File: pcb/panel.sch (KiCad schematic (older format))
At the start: 15 parts, among them IC1 ATMEGA88P-20PU, P1 KEYBOARD, P2 SERIAL, P3 I2C, U1 C, U2 CP, U3 2X16DIGIT-DISPLAY

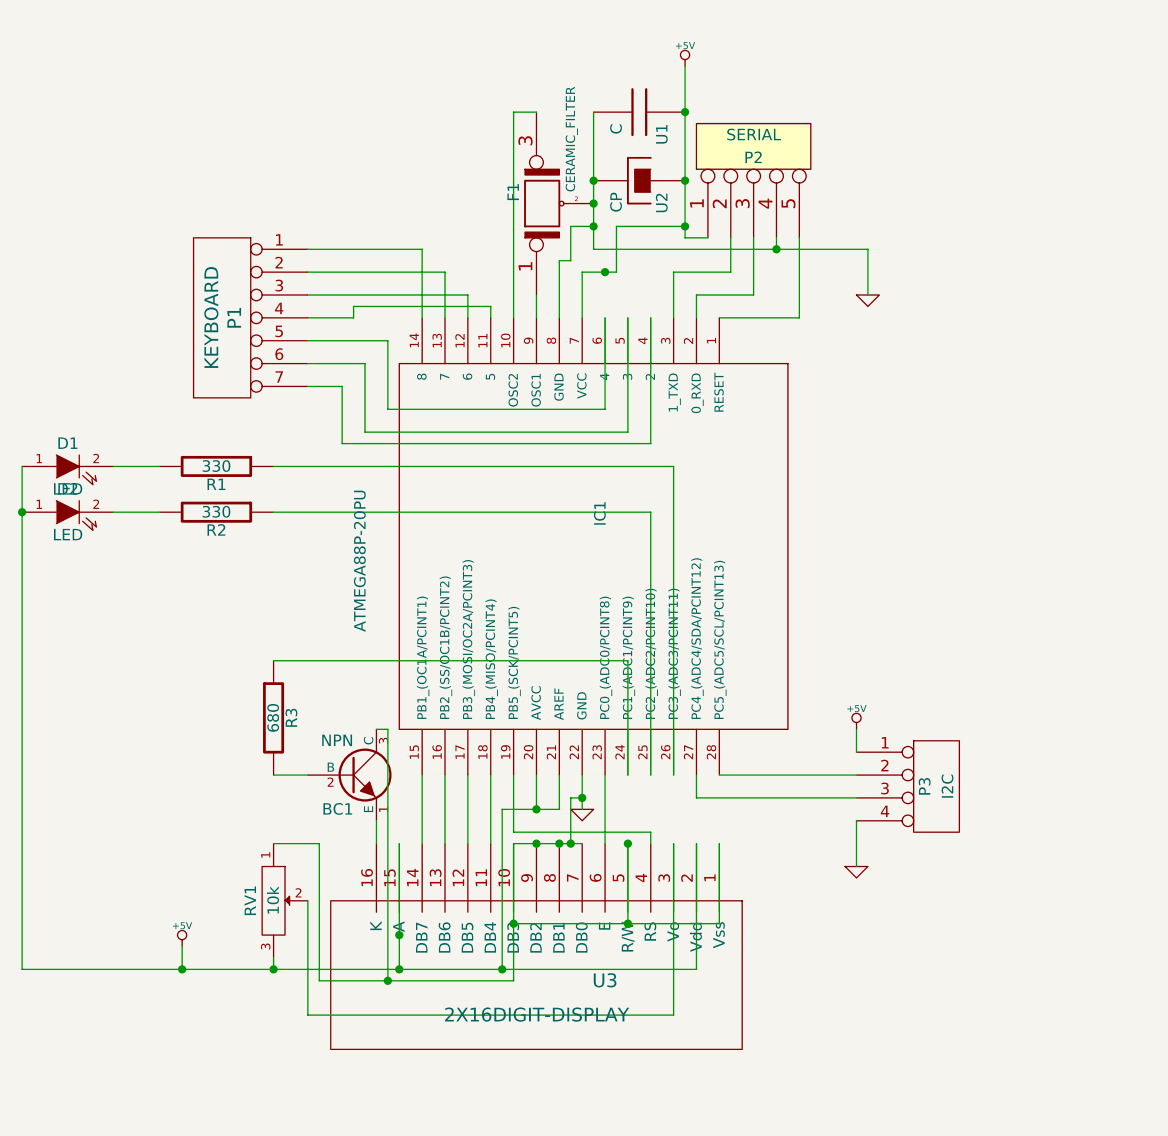
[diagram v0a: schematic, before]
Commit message: new i2cpanel with buttons onboard instead of external keyboard rev 0.3
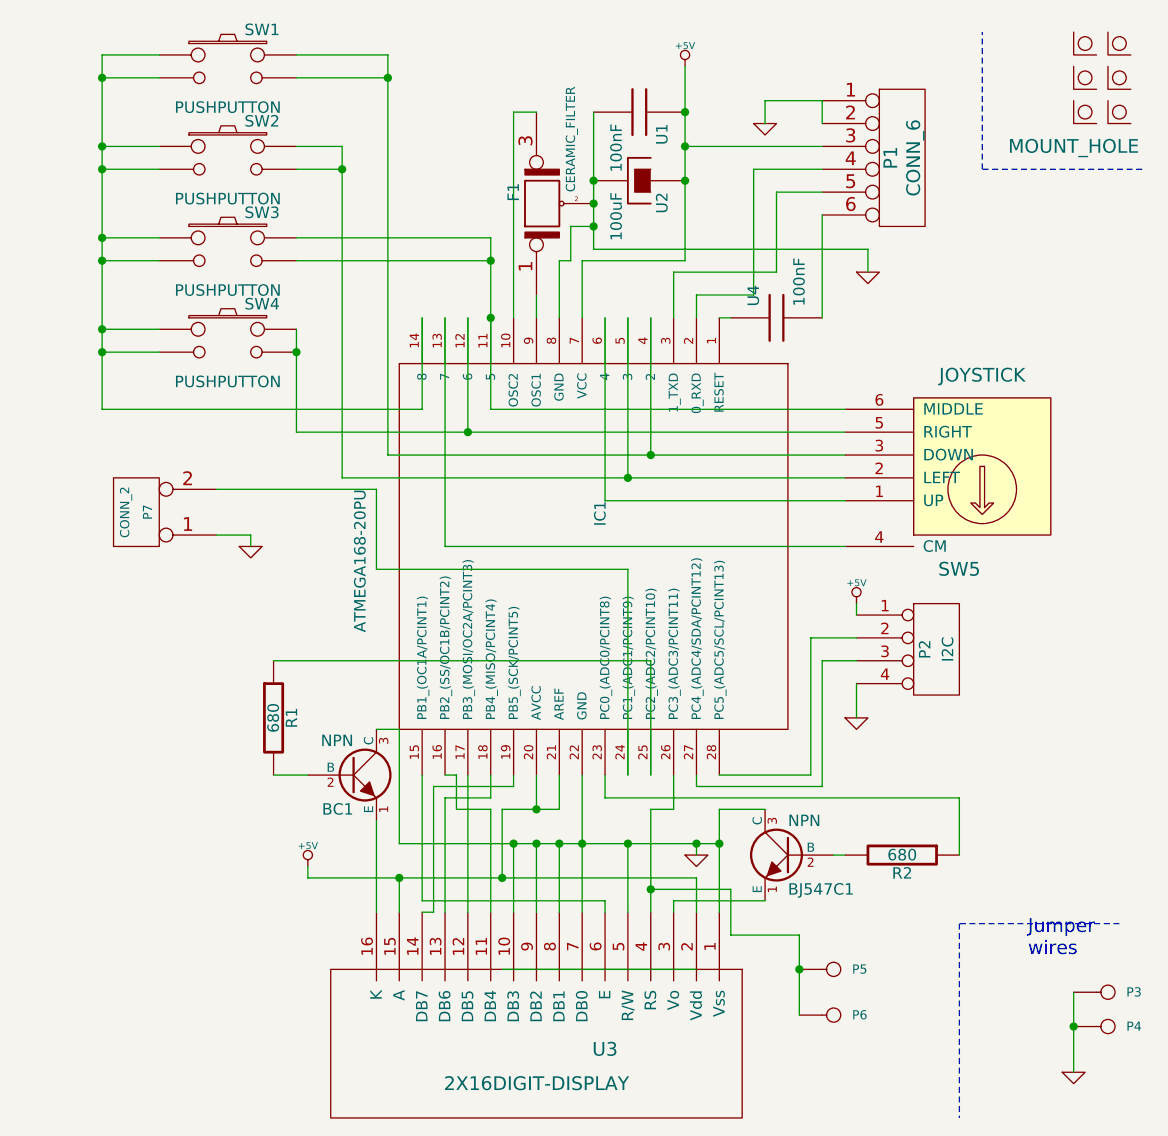
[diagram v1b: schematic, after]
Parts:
- removed D1, D2: LED, symbol LED
- removed P1: KEYBOARD, symbol CONN_7
- removed P2: SERIAL, symbol CONN_5
- removed R1: 330, symbol R
- removed RV1: 10k, symbol POT
- added BJ547C1: NPN, symbol NPN
- added H1, H2, H3, H4, H5, H6: MOUNT_HOLE, symbol MOUNT_HOLE
- added P1: CONN_6, symbol CONN_6
- added P3, P4, P5, P6: CONN_1, symbol CONN_1
- added P7: CONN_2, symbol CONN_2
- added SW1, SW2, SW3, SW4: PUSHPUTTON, symbol PUSHPUTTON
- added SW5: JOYSTICK, symbol JOYSTICK
- added U4: 100nF, symbol C
- IC1: value ATMEGA88P-20PU -> ATMEGA168-20PU
- R2: value 330 -> 680
- U1: value C -> 100nF
- U2: value CP -> 100uF
- renumbered P3 to P2, R3 to R1
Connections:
- net +5V: now also P1.3
- net GND: now also BJ547C1.3 (C), P1.1, P1.2, P3.1, P4.1, P7.1 (P1)
- net at IC1.1 (RESET): now also U4.1
- net at IC1.11 (5): now also SW3.3, SW3.4, SW5.6 (MIDDLE)
- net at IC1.12 (6): now also SW4.3, SW4.4, SW5.5 (RIGHT)
- net at IC1.13 (7): now also SW5.4 (CM)
- net at IC1.14 (8): now also SW1.1, SW1.2, SW2.1, SW2.2, SW3.1, SW3.2, SW4.1, SW4.2
- net at IC1.15 (PB1_(OC1A/PCINT1)): now also U3.6 (E); no longer U3.14 (DB7)
- net at IC1.16 (PB2_(SS/OC1B/PCINT2)): now also U3.11 (DB4); no longer U3.13 (DB6)
- net at IC1.18 (PB4_(MISO/PCINT4)): now also U3.13 (DB6); no longer U3.11 (DB4)
- net at IC1.19 (PB5_(SCK/PCINT5)): now also U3.14 (DB7); no longer U3.4 (RS)
- net at IC1.2 (0_RXD): now also P1.4
- net at IC1.23 (PC0_(ADC0/PCINT8)): now also R2.1; no longer U3.6 (E)
- net at IC1.24 (PC1_(ADC1/PCINT9)): now also P7.2 (PM); no longer R1.1
- net at IC1.25 (PC2_(ADC2/PCINT10)): now also R1.1; no longer R2.1
- net at IC1.26 (PC3_(ADC3/PCINT11)): now also U3.4 (RS), P5.1, P6.1
- net at IC1.3 (1_TXD): now also P1.5
- net at IC1.4 (2): now also SW1.3, SW1.4, SW5.3 (DOWN)
- net at IC1.5 (3): now also SW2.3, SW2.4, SW5.2 (LEFT)
- net at IC1.6 (4): now also SW5.1 (UP)
- net at U3.3 (Vo): now also BJ547C1.1 (E)
- net at R2.2: now also BJ547C1.2 (B)
- new net: P1.6, U4.2
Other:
- note added: "Jumper\nwires"
- moved on the sheet: P2, U3
